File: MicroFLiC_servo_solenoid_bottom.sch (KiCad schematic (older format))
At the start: 10 parts, among them P1 1x14 header strip, P10 1x4 socket strip, P2 1x14 socket strip, P3 12-way Micro-MaTch, P4 Jack_3.5mm_3pin, P5 Jack_3.5mm_3pin, P6 RCA_3, P7 RCA_3, P8 1x6 socket strip, P9 1x4 header strip

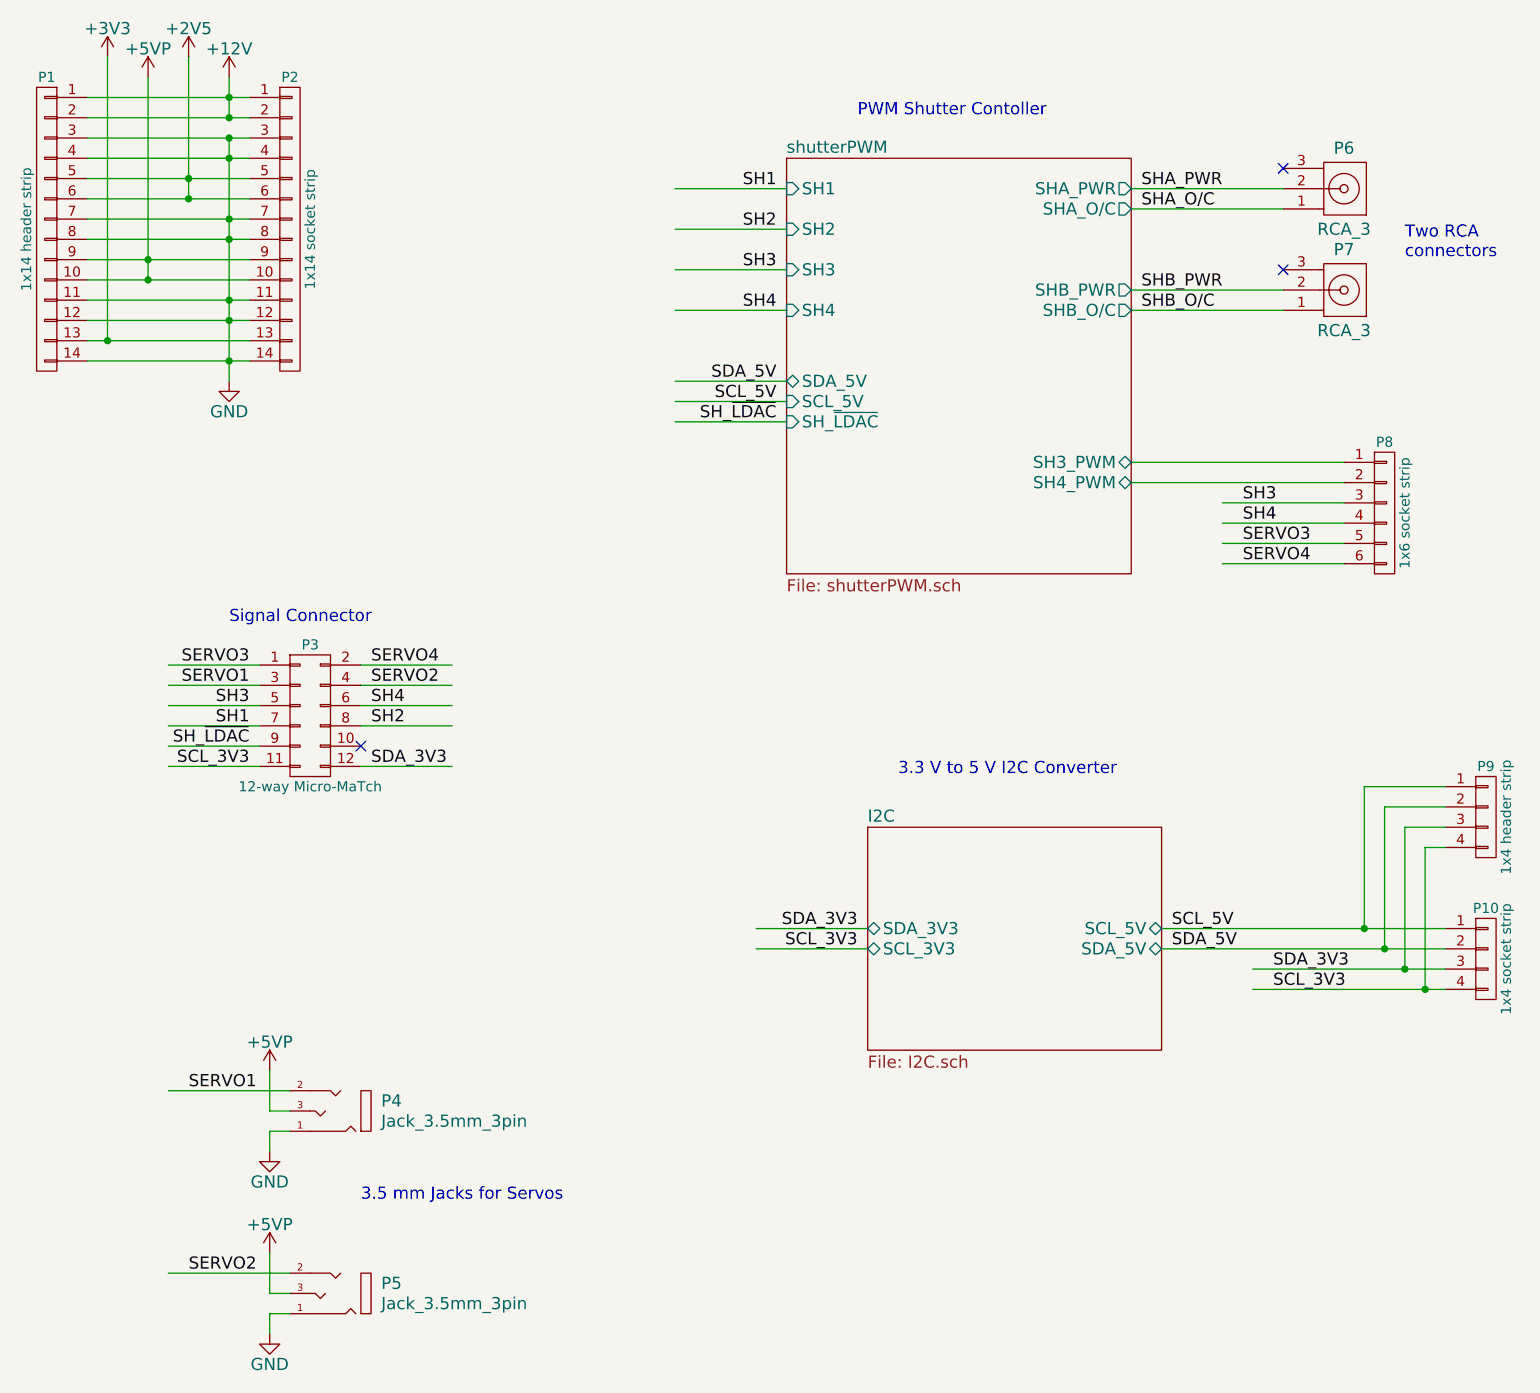
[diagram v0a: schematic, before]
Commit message: Fixed jack part values
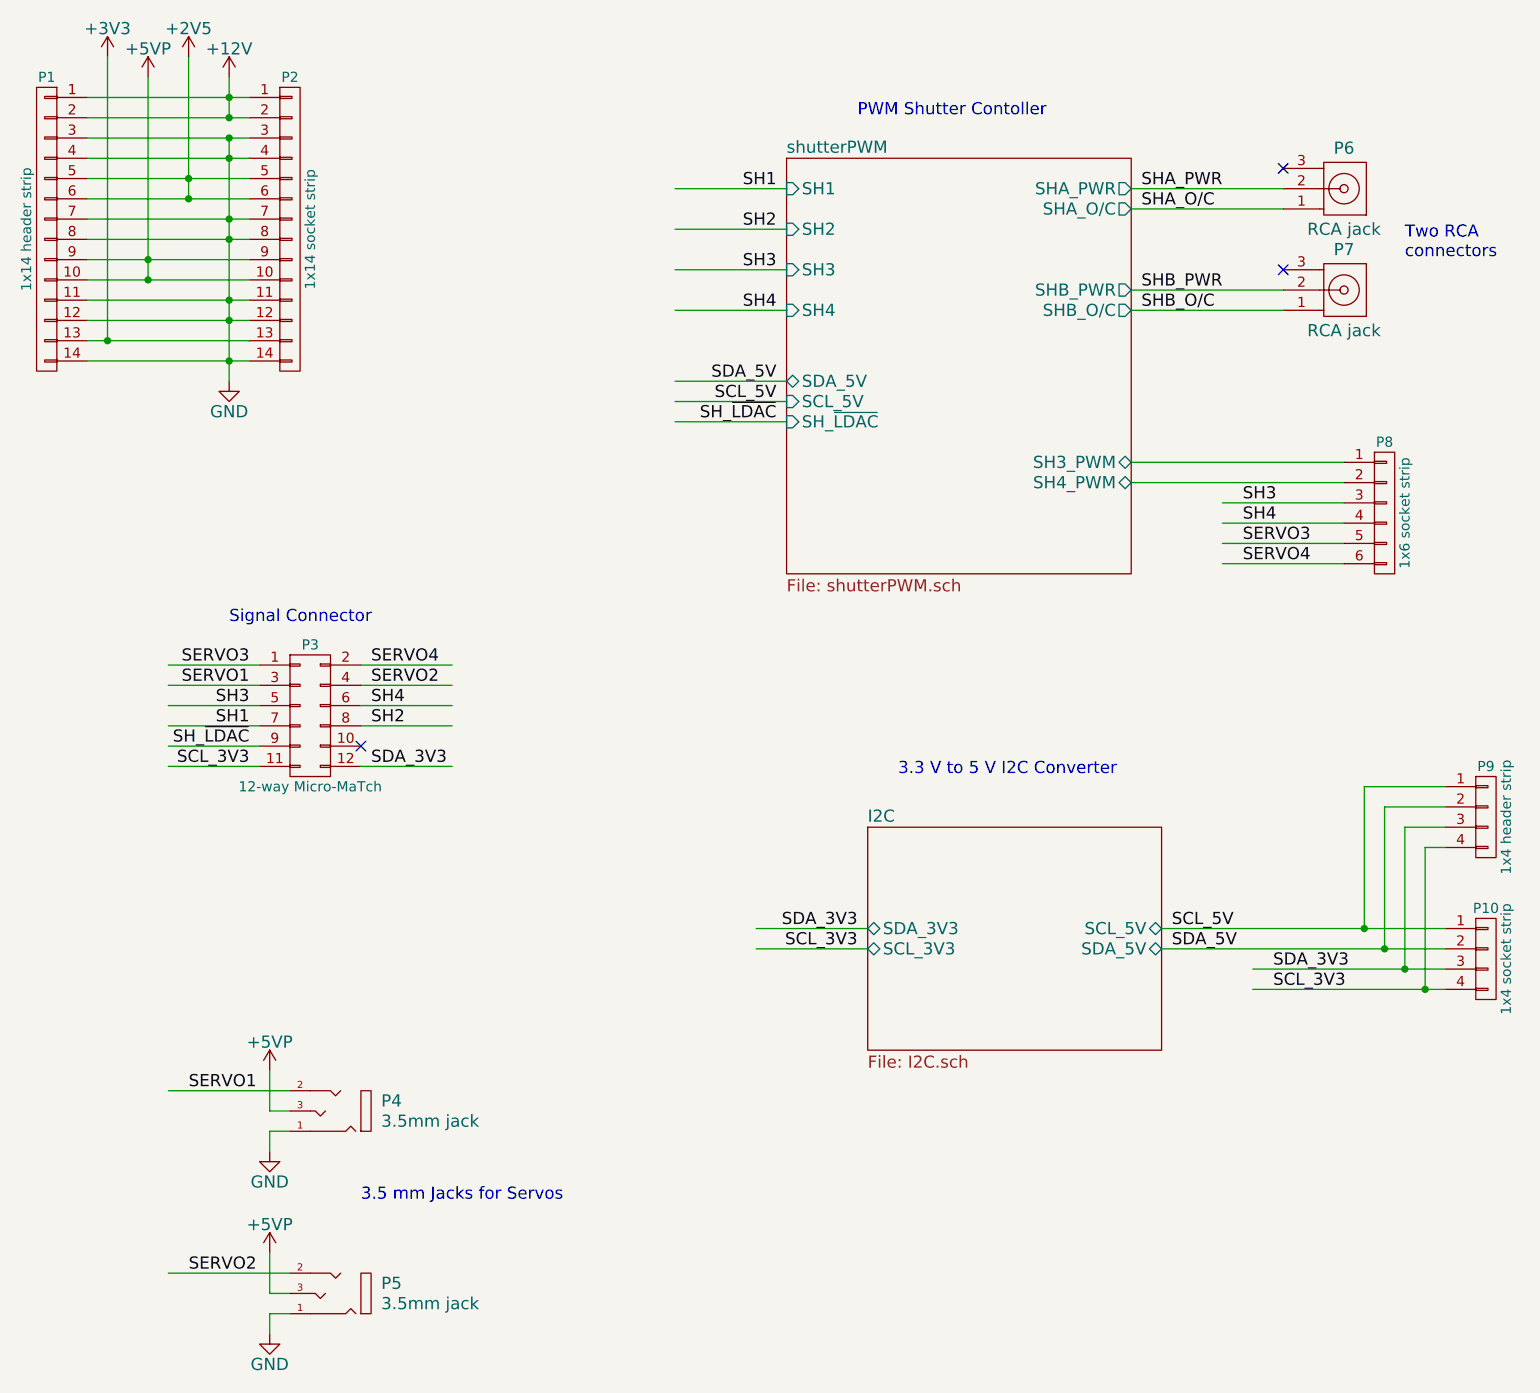
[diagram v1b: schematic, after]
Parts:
- P4, P5: value Jack_3.5mm_3pin -> 3.5mm jack
- P6, P7: value RCA_3 -> RCA jack
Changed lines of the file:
@@
 P 2700 6250
 F 0 "P4" H 2450 6250 60  0000 R CNN
-F 1 "Jack_3.5mm_3pin" H 2450 6350 60  0000 R CNN
+F 1 "3.5mm jack" H 2450 6350 60  0000 R CNN
 F 2 "jakub:MJ4435-R" H 2675 6250 60  0001 C CNN
 F 3 "" H 2675 6250 60  0000 C CNN
@@
 P 7700 2250
 F 0 "P7" H 7700 2450 60  0000 C CNN
-F 1 "RCA_3" H 7700 2050 60  0000 C CNN
+F 1 "RCA jack" H 7700 2050 60  0000 C CNN
 F 2 "jakub:PSG01544" H 7700 2250 60  0001 C CNN
 F 3 "" H 7700 2250 60  0000 C CNN
@@
 P 7700 1750
 F 0 "P6" H 7700 1950 60  0000 C CNN
-F 1 "RCA_3" H 7700 1550 60  0000 C CNN
+F 1 "RCA jack" H 7700 1550 60  0000 C CNN
 F 2 "jakub:PSG01544" H 7700 1750 60  0001 C CNN
 F 3 "" H 7700 1750 60  0000 C CNN
@@
 P 2700 7150
 F 0 "P5" H 2450 7150 60  0000 R CNN
-F 1 "Jack_3.5mm_3pin" H 2450 7250 60  0000 R CNN
+F 1 "3.5mm jack" H 2450 7250 60  0000 R CNN
 F 2 "jakub:MJ4435-R" H 2675 7150 60  0001 C CNN
 F 3 "" H 2675 7150 60  0000 C CNN

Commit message: Fixed jack part values
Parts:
- P4, P5, P6, P7: Alt. Order Code (none) -> N/A
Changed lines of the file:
@@
 F 8 "1638670" H 2700 6250 60  0001 C CNN "Order Code"
 F 9 "N/A" H 2700 6250 60  0001 C CNN "Alt. Supplier"
-F 10 "Right-angle SMD 3.5mm 3-pin jack" H 2700 6250 60  0001 C CNN "Note"
+F 10 "N/A" H 2700 6250 60  0001 C CNN "Alt. Order Code"
+F 11 "Right-angle SMD 3.5mm 3-pin jack" H 2700 6250 60  0001 C CNN "Note"
 	1    2700 6250
 	-1   0    0    1
@@
 F 8 "1280698" H 7700 2250 60  0001 C CNN "Order Code"
 F 9 "N/A" H 7700 2250 60  0001 C CNN "Alt. Supplier"
-F 10 "Right-angle RCA jack" H 7700 2250 60  0001 C CNN "Note"
+F 10 "N/A" H 7700 2250 60  0001 C CNN "Alt. Order Code"
+F 11 "Right-angle RCA jack" H 7700 2250 60  0001 C CNN "Note"
 	1    7700 2250
 	1    0    0    -1
@@
 F 8 "1280698" H 7700 1750 60  0001 C CNN "Order Code"
 F 9 "N/A" H 7700 1750 60  0001 C CNN "Alt. Supplier"
-F 10 "Right-angle RCA jack" H 7700 1750 60  0001 C CNN "Note"
+F 10 "N/A" H 7700 1750 60  0001 C CNN "Alt. Order Code"
+F 11 "Right-angle RCA jack" H 7700 1750 60  0001 C CNN "Note"
 	1    7700 1750
 	1    0    0    -1
@@
 F 8 "1638670" H 2700 7150 60  0001 C CNN "Order Code"
 F 9 "N/A" H 2700 7150 60  0001 C CNN "Alt. Supplier"
-F 10 "Right-angle SMD 3.5mm 3-pin jack" H 2700 7150 60  0001 C CNN "Note"
+F 10 "N/A" H 2700 7150 60  0001 C CNN "Alt. Order Code"
+F 11 "Right-angle SMD 3.5mm 3-pin jack" H 2700 7150 60  0001 C CNN "Note"
 	1    2700 7150
 	-1   0    0    1
